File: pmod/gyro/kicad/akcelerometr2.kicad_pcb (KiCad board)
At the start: 4 copper layers, 27 x 22.5 mm, 5 parts, among them J2 Conn_01x04_Pin, J3 Conn_01x04_Pin, J4 Conn_01x08_Pin

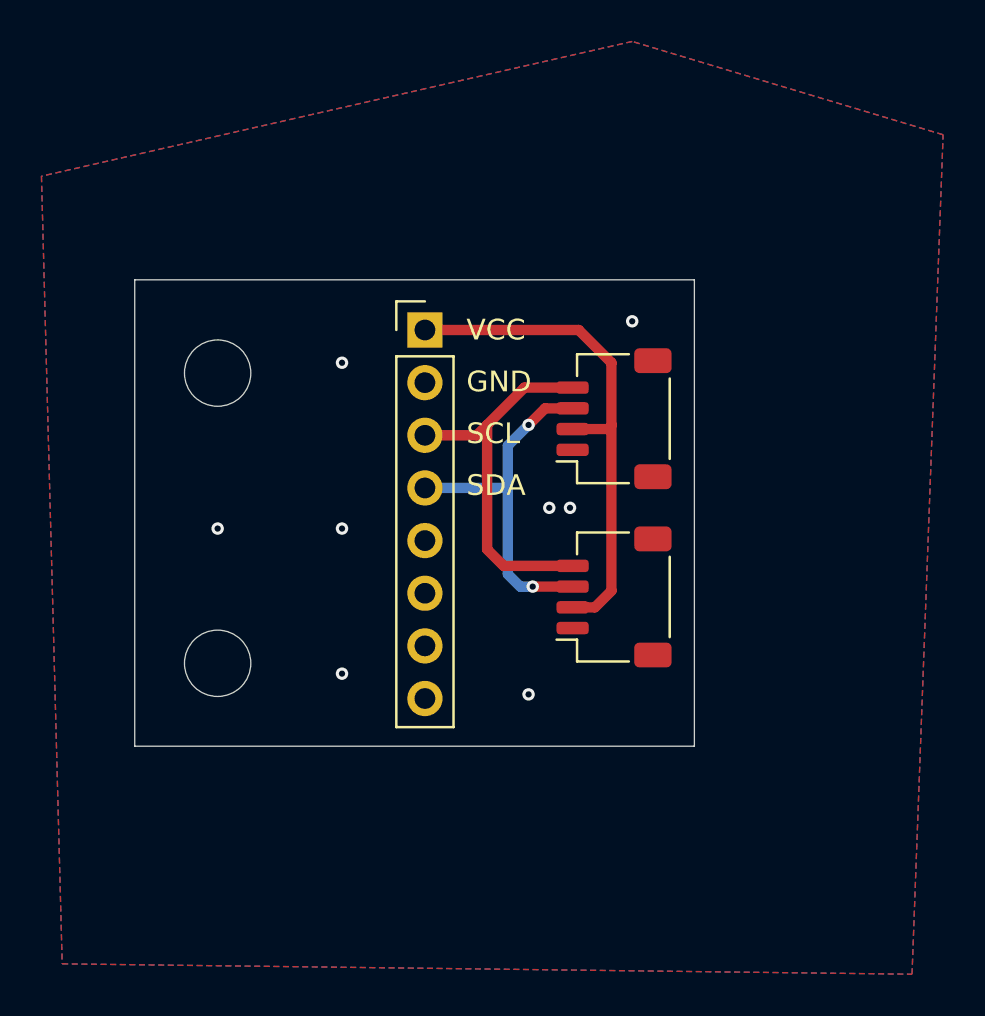
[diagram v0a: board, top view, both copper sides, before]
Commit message: Oprava v modulu gyro
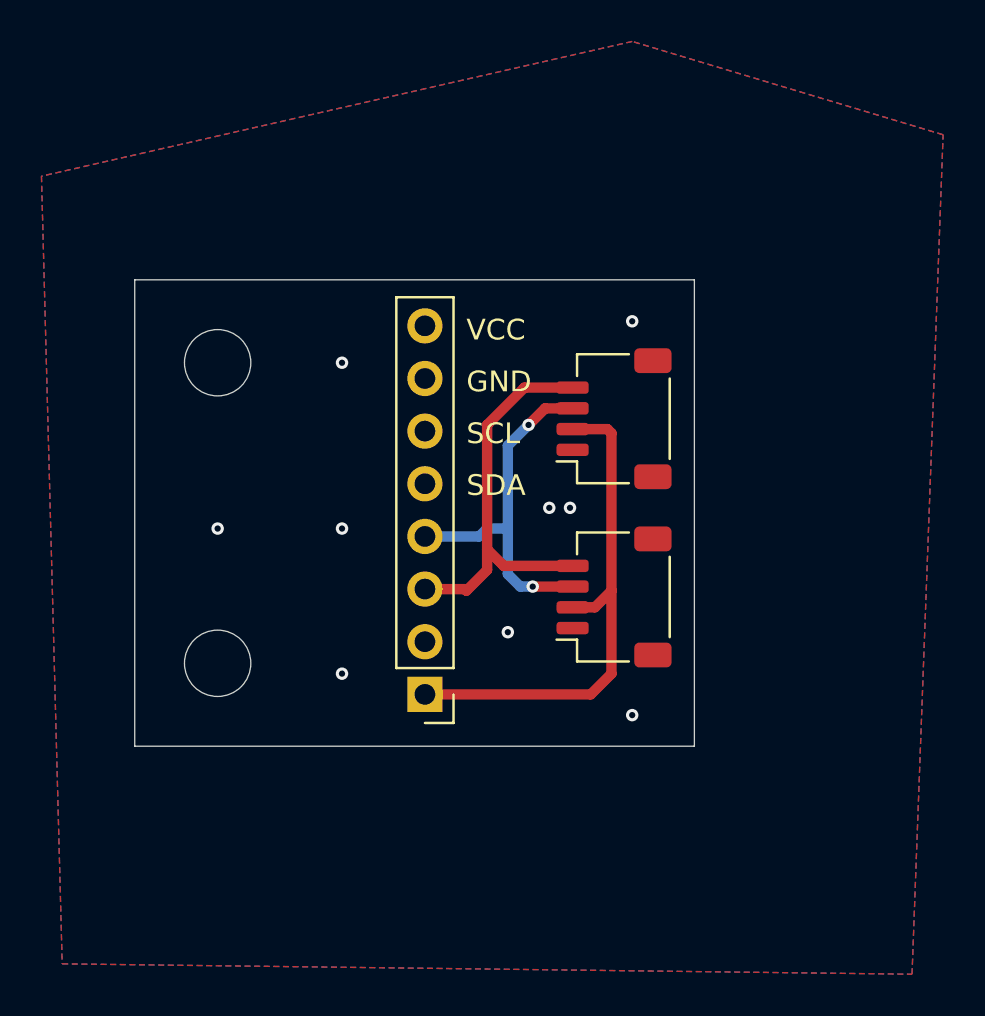
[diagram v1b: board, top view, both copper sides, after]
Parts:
- moved J4 17.6 mm to (134.0, 105.0), turned to 180 degrees
- moved H2 0.50 mm to (124.0, 89.0)
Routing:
- net Net-(J2-Pin_4): track 18.5 -> 19.8 mm
- net GND: vias 8 -> 9

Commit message: fix
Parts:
- moved H2 17.0 mm to (139.0, 81.0)
- moved H1 16.8 mm to (139.0, 111.0)
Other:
- board size 27 x 22.5 mm -> 16 x 37.5 mm
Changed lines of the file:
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@@
 	(footprint "MountingHole:MountingHole_3.2mm_M3"
 		(layer "F.Cu")
-		(at 124 89)
+		(at 139 81)
 		(descr "Mounting Hole 3.2mm, M3, no annular, generated by kicad-footprint-generator mountinghole.py")
 		(tags "mountinghole M3")
@@
 	(footprint "MountingHole:MountingHole_3.2mm_M3"
 		(layer "F.Cu")
-		(at 124 103.5)
+		(at 139 111)
 		(descr "Mounting Hole 3.2mm, M3, no annular, generated by kicad-footprint-generator mountinghole.py")
 		(tags "mountinghole M3")
@@
 	)
 	(gr_rect
-		(start 120 85)
-		(end 147 107.5)
+		(start 131 77)
+		(end 147 114.5)
 		(stroke
 			(width 0.05)
@@
 	)
 	(gr_text "VCC\n"
-		(at 136 88 0)
+		(at 135.7 105.6 0)
 		(layer "F.SilkS")
 		(effects
@@
 	)
 	(gr_text "SCL\n"
-		(at 136 93 0)
+		(at 135.6 100.4 0)
 		(layer "F.SilkS")
 		(effects
@@
 	)
 	(gr_text "SDA"
-		(at 136 95.5 0)
+		(at 135.6 98 0)
 		(layer "F.SilkS")
 		(effects
@@
 	)
 	(gr_text "GND"
-		(at 136 90.5 0)
+		(at 135.6 103 0)
 		(layer "F.SilkS")
 		(effects
@@
 	)
 	(via
-		(at 144 106)
+		(at 144.6 81.1)
 		(size 0.6)
 		(drill 0.3)
@@
 	)
 	(via
-		(at 130 104)
+		(at 134 81)
+		(size 0.6)
+		(drill 0.3)
+		(layers "F.Cu" "B.Cu")
+		(free yes)
+		(net 1)
+	)
+	(via
+		(at 142.5 107.1)
+		(size 0.6)
+		(drill 0.3)
+		(layers "F.Cu" "B.Cu")
+		(free yes)
+		(net 1)
+	)
+	(via
+		(at 144.4 111.4)
 		(size 0.6)
 		(drill 0.3)
@@
 	)
 	(via
-		(at 144 87)
+		(at 142 86)
 		(size 0.6)
 		(drill 0.3)
@@
 	)
 	(via
-		(at 140 96)
+		(at 139.3 95.1)
 		(size 0.6)
 		(drill 0.3)
@@
 	)
 	(via
-		(at 124 97)
+		(at 140.1 103.4)
 		(size 0.6)
 		(drill 0.3)
@@
 	)
 	(via
-		(at 138 102)
+		(at 133.5 111.5)
 		(size 0.6)
 		(drill 0.3)
@@
 		(net 1)
 	)
-	(via
-		(at 130 97)
-		(size 0.6)
-		(drill 0.3)
-		(layers "F.Cu" "B.Cu")
-		(free yes)
-		(net 1)
-	)
-	(via
-		(at 130 89)
-		(size 0.6)
-		(drill 0.3)
-		(layers "F.Cu" "B.Cu")
-		(free yes)
-		(net 1)
-	)
 	(segment
 		(start 143 92.4)
@@
 	)
 	(segment
-		(start 137 99)
-		(end 136 100)
-		(width 0.5)
-		(layer "F.Cu")
-		(net 4)
-	)
-	(segment
 		(start 137.8 98.8)
 		(end 141.125 98.8)
@@
 	)
 	(segment
-		(start 136 100)
-		(end 135.92 99.92)
+		(start 137 99)
+		(end 136.08 99.92)
+		(width 0.5)
+		(layer "F.Cu")
+		(net 4)
+	)
+	(segment
+		(start 136.08 99.92)
+		(end 134 99.92)
 		(width 0.5)
 		(layer "F.Cu")
@@
 		(width 0.5)
 		(layer "F.Cu")
-		(net 4)
-	)
-	(segment
-		(start 135.92 99.92)
-		(end 134 99.92)
-		(width 0.5)
-		(layer "F.Cu")

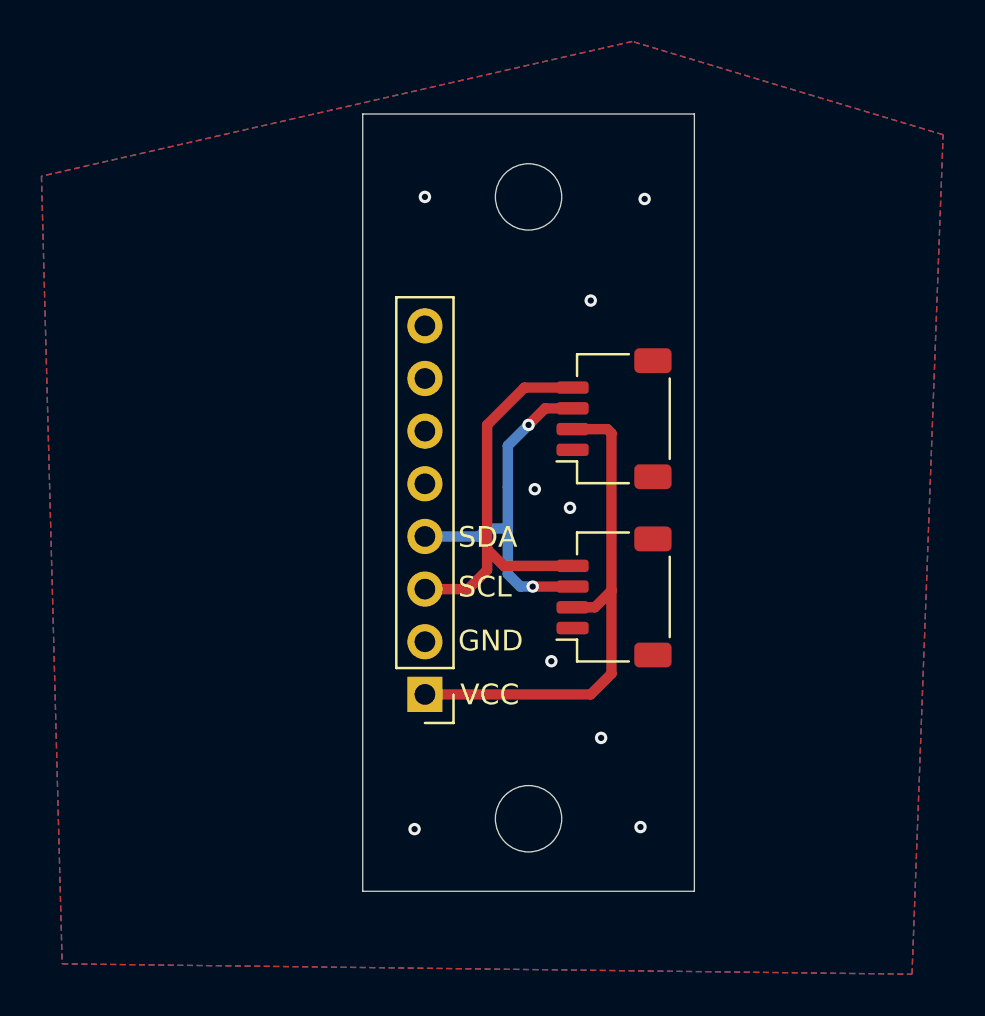
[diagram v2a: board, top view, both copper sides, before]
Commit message: Added link and logo to front and back. Added hole labels and dimensions
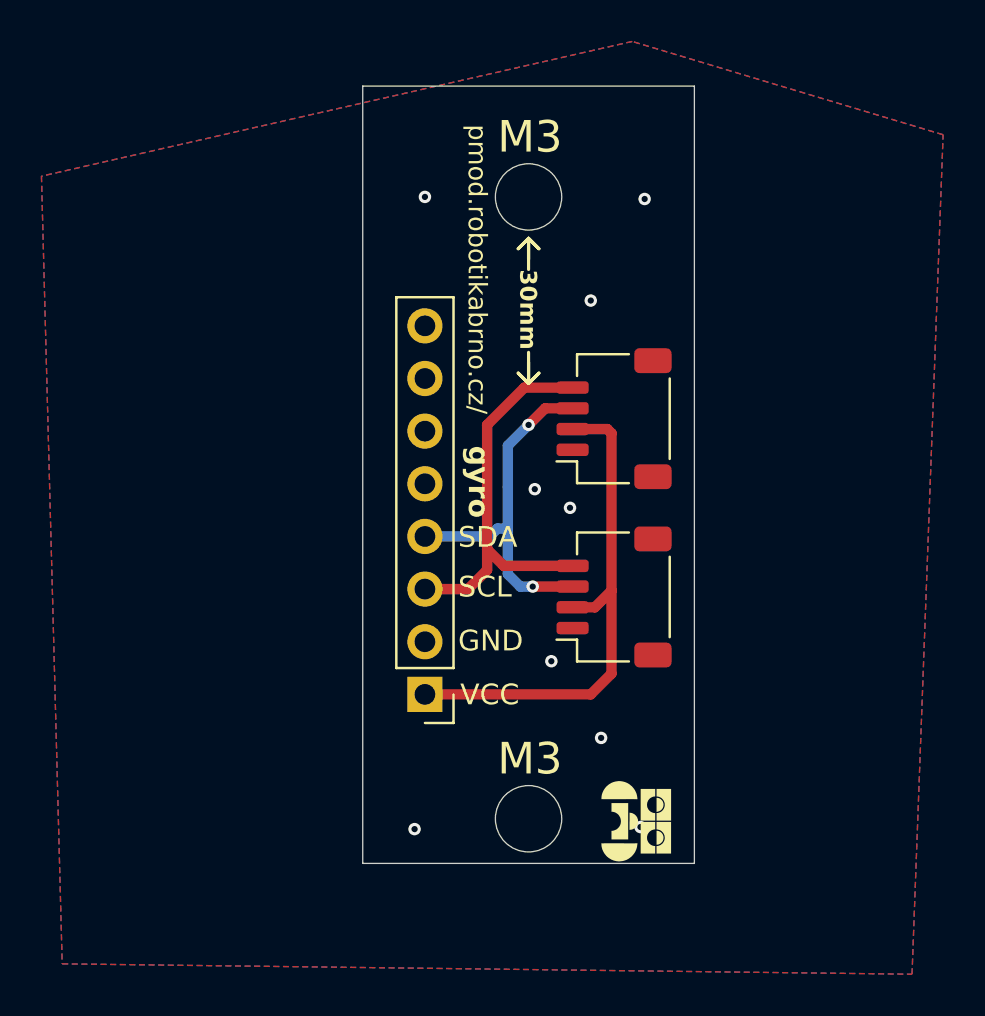
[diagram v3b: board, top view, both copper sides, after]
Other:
- board text added: "30mm"
- board text added: "M3"
- board text added: "gyro"
- board text added: "pmod.robotikabrno.cz/"

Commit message: layer count change + minor fixes
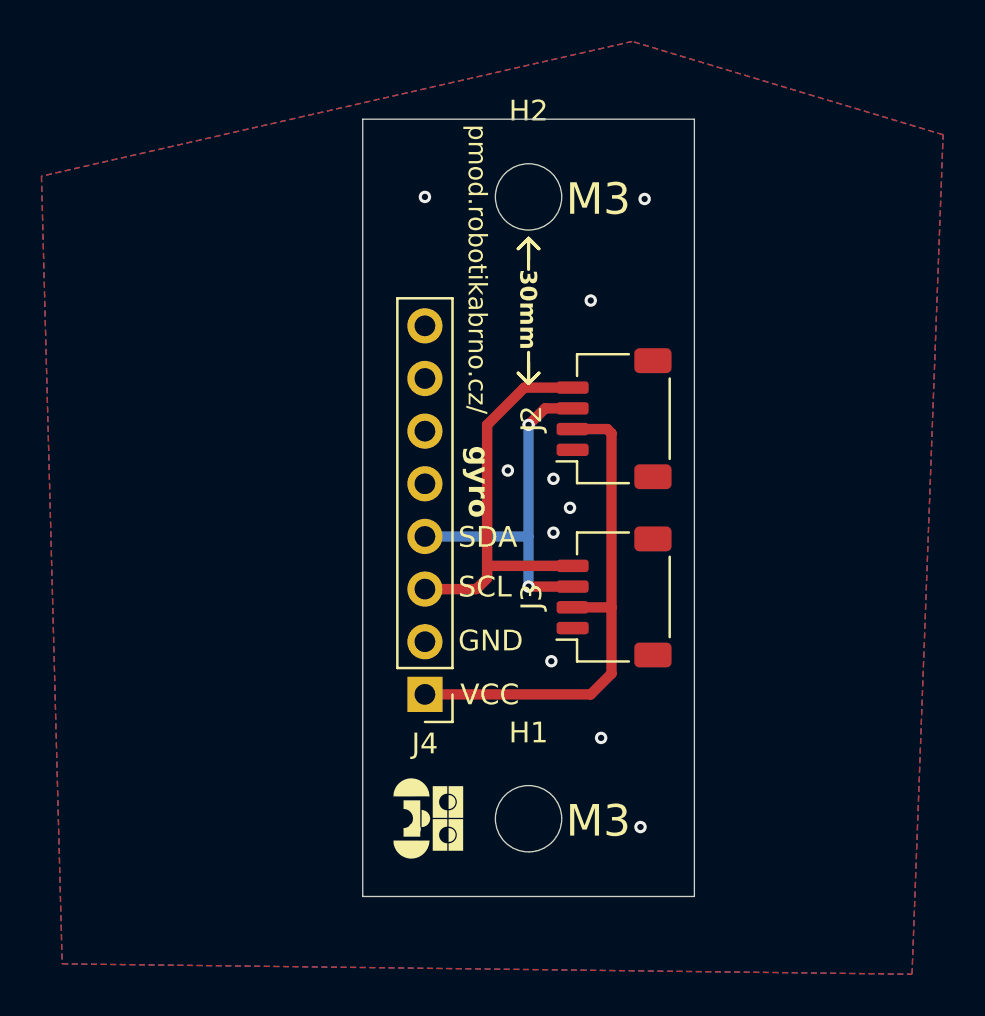
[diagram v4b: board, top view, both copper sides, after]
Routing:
- net GND: vias 9 -> 11
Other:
- copper layers 4 -> 2
